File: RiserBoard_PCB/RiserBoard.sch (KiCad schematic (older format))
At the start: 11 parts, among them J1 BUS1, J2 Input, J3 BUS2

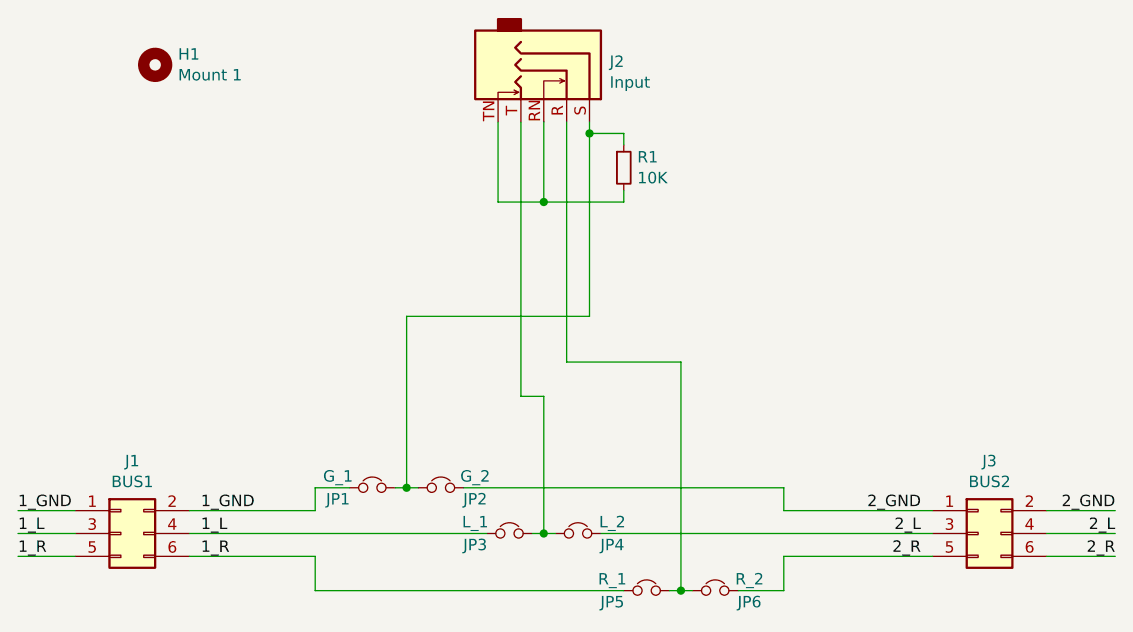
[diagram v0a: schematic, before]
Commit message: Updated Design to v0.1
Smaller PCB
Only 1 sided PCB
Different Jack Footprint
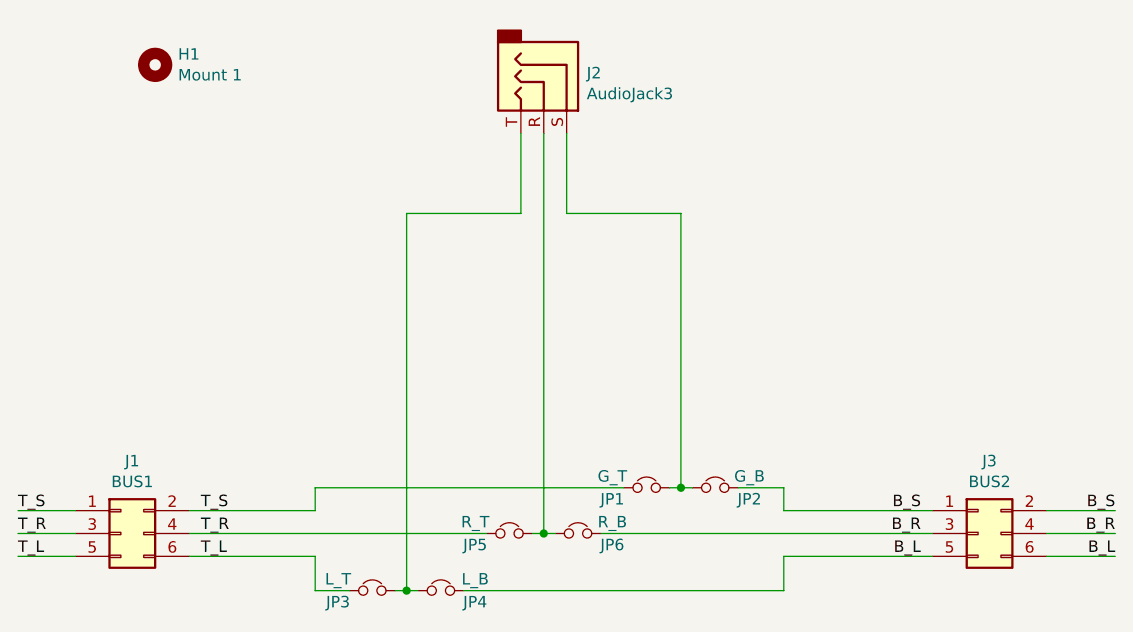
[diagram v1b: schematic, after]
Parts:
- removed J2: Input, Jack_3.5mm_Switchcraft_35RASMT4BHNTRX:Jack_3.5mm_Switchcraft_35RASMT4BHNTRX, symbol Connector:AudioJack3_SwitchTR
- removed R1: 10K, Resistor_SMD:R_0603_1608Metric, symbol Device:R_Small
- added J2: AudioJack3, Jack_3.5mm_PJ-313D-6A:PJ-313D-6A, symbol Connector:AudioJack3
- JP1: value G_1 -> G_T
- JP2: value G_2 -> G_B
- JP3: value L_1 -> L_T
- JP4: value L_2 -> L_B
- JP5: value R_1 -> R_T
- JP6: value R_2 -> R_B
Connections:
- net at JP1.2, JP2.1: now also J2.S
- net at JP3.2, JP4.1: now also J2.T
- net at JP5.2, JP6.1: now also J2.R
- net 1_GND renamed T_S
- net 1_L renamed T_R
- net T_R: now also JP5.1; no longer JP3.1
- net 1_R renamed T_L
- net T_L: now also JP3.1; no longer JP5.1
- net 2_GND renamed B_S
- net 2_L renamed B_R
- net B_R: now also JP6.2; no longer JP4.2
- net 2_R renamed B_L
- net B_L: now also JP4.2; no longer JP6.2
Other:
- moved on the sheet: JP1, JP2, JP3, JP4, JP5, JP6
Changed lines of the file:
@@
 	2950 4300 2700 4300
 Text Label 2700 4100 0    50   ~ 0
-1_GND
+T_S
 Text Label 2700 4200 0    50   ~ 0
-1_L
+T_R
 Text Label 2700 4300 0    50   ~ 0
-1_R
+T_L
 Text Label 3500 4100 0    50   ~ 0
-1_GND
+T_S
 Text Label 3500 4200 0    50   ~ 0
-1_L
+T_R
 Text Label 3500 4300 0    50   ~ 0
-1_R
+T_L
 Text Label 7500 4300 2    50   ~ 0
-2_R
-Text Label 7500 4200 2    50   ~ 0
-2_L
+B_L
 Text Label 7500 4100 2    50   ~ 0
-2_GND
+B_S
 Wire Wire Line
 	7200 4100 7500 4100
@@
 	7200 4300 7500 4300
 Text Label 6650 4300 2    50   ~ 0
-2_R
+B_L
 Text Label 6650 4200 2    50   ~ 0
-2_L
+B_R
 Text Label 6650 4100 2    50   ~ 0
-2_GND
-Wire Wire Line
-	4150 4000 4000 4000
+B_S
 Wire Wire Line
 	4000 4000 4000 4100
-Wire Wire Line
-	5350 4450 4000 4450
 Wire Wire Line
 	4000 4450 4000 4300
@@
 	6050 4000 6050 4100
 Wire Wire Line
-	6050 4450 6050 4300
-Wire Wire Line
 	3450 4100 4000 4100
-Wire Wire Line
-	3450 4200 4750 4200
 Wire Wire Line
 	3450 4300 4000 4300
@@
 L Device:Jumper_NC_Small JP1
 U 1 1 5E7C1BD8
-P 4250 4000
-F 0 "JP1" H 4100 3950 50  0000 C CNN
-F 1 "G_1" H 4100 4050 50  0000 C CNN
-F 2 "Resistor_SMD:R_0603_1608Metric" H 4250 4000 50  0001 C CNN
-F 3 "~" H 4250 4000 50  0001 C CNN
-	1    4250 4000
+P 5450 4000
+F 0 "JP1" H 5300 3950 50  0000 C CNN
+F 1 "G_T" H 5300 4050 50  0000 C CNN
+F 2 "Resistor_SMD:R_0603_1608Metric" H 5450 4000 50  0001 C CNN
+F 3 "~" H 5450 4000 50  0001 C CNN
+	1    5450 4000
 	1    0    0    -1
 $EndComp
@@
 L Device:Jumper_NC_Small JP2
 U 1 1 5E7C23FE
-P 4550 4000
-F 0 "JP2" H 4700 3950 50  0000 C CNN
-F 1 "G_2" H 4700 4050 50  0000 C CNN
-F 2 "Resistor_SMD:R_0603_1608Metric" H 4550 4000 50  0001 C CNN
-F 3 "~" H 4550 4000 50  0001 C CNN
-	1    4550 4000
+P 5750 4000
+F 0 "JP2" H 5900 3950 50  0000 C CNN
+F 1 "G_B" H 5900 4050 50  0000 C CNN
+F 2 "Resistor_SMD:R_0603_1608Metric" H 5750 4000 50  0001 C CNN
+F 3 "~" H 5750 4000 50  0001 C CNN
+	1    5750 4000
 	1    0    0    -1
 $EndComp
-Wire Wire Line
-	4350 4000 4400 4000
 $Comp
 L Device:Jumper_NC_Small JP3
 U 1 1 5E7C4C9C
+P 4250 4450
+F 0 "JP3" H 4100 4400 50  0000 C CNN
+F 1 "L_T" H 4100 4500 50  0000 C CNN
+F 2 "Resistor_SMD:R_0603_1608Metric" H 4250 4450 50  0001 C CNN
+F 3 "~" H 4250 4450 50  0001 C CNN
+	1    4250 4450
+	1    0    0    -1
+$EndComp
+$Comp
+L Device:Jumper_NC_Small JP4
+U 1 1 5E7C4CA2
+P 4550 4450
+F 0 "JP4" H 4700 4400 50  0000 C CNN
+F 1 "L_B" H 4700 4500 50  0000 C CNN
+F 2 "Resistor_SMD:R_0603_1608Metric" H 4550 4450 50  0001 C CNN
+F 3 "~" H 4550 4450 50  0001 C CNN
+	1    4550 4450
+	1    0    0    -1
+$EndComp
+$Comp
+L Device:Jumper_NC_Small JP5
+U 1 1 5E7C8F61
 P 4850 4200
-F 0 "JP3" H 4700 4150 50  0000 C CNN
-F 1 "L_1" H 4700 4250 50  0000 C CNN
+F 0 "JP5" H 4700 4150 50  0000 C CNN
+F 1 "R_T" H 4700 4250 50  0000 C CNN
 F 2 "Resistor_SMD:R_0603_1608Metric" H 4850 4200 50  0001 C CNN
 F 3 "~" H 4850 4200 50  0001 C CNN
@@
 $EndComp
 $Comp
-L Device:Jumper_NC_Small JP4
-U 1 1 5E7C4CA2
+L Device:Jumper_NC_Small JP6
+U 1 1 5E7C8F67
 P 5150 4200
-F 0 "JP4" H 5300 4150 50  0000 C CNN
-F 1 "L_2" H 5300 4250 50  0000 C CNN
+F 0 "JP6" H 5300 4150 50  0000 C CNN
+F 1 "R_B" H 5300 4250 50  0000 C CNN
 F 2 "Resistor_SMD:R_0603_1608Metric" H 5150 4200 50  0001 C CNN
 F 3 "~" H 5150 4200 50  0001 C CNN
@@
 	1    0    0    -1
 $EndComp
-$Comp
-L Device:Jumper_NC_Small JP5
-U 1 1 5E7C8F61
-P 5450 4450
-F 0 "JP5" H 5300 4400 50  0000 C CNN
-F 1 "R_1" H 5300 4500 50  0000 C CNN
-F 2 "Resistor_SMD:R_0603_1608Metric" H 5450 4450 50  0001 C CNN
-F 3 "~" H 5450 4450 50  0001 C CNN
-	1    5450 4450
-	1    0    0    -1
-$EndComp
-$Comp
-L Device:Jumper_NC_Small JP6
-U 1 1 5E7C8F67
-P 5750 4450
-F 0 "JP6" H 5900 4400 50  0000 C CNN
-F 1 "R_2" H 5900 4500 50  0000 C CNN
-F 2 "Resistor_SMD:R_0603_1608Metric" H 5750 4450 50  0001 C CNN
-F 3 "~" H 5750 4450 50  0001 C CNN
-	1    5750 4450
-	1    0    0    -1
-$EndComp
-Connection ~ 4400 4000
-Wire Wire Line
-	4400 4000 4450 4000
 $Comp
 L Connector_Generic:Conn_02x03_Odd_Even J1
@@
 	1    0    0    -1
 $EndComp
+$Comp
+L Connector:AudioJack3 J2
+U 1 1 5EC1880E
+P 5000 2250
+F 0 "J2" V 4936 2438 50  0000 L CNN
+F 1 "AudioJack3" V 5027 2438 50  0000 L CNN
+F 2 "Jack_3.5mm_PJ-313D-6A:PJ-313D-6A" H 5000 2250 50  0001 C CNN
+F 3 "~" H 5000 2250 50  0001 C CNN
+	1    5000 2250
+	0    1    1    0
+$EndComp
+Wire Wire Line
+	6050 4450 6050 4300
+Text Label 7500 4200 2    50   ~ 0
+B_R
+Wire Wire Line
+	5550 4000 5600 4000
+Wire Wire Line
+	4950 4200 5000 4200
+Wire Wire Line
+	4350 4450 4400 4450
+Wire Wire Line
+	4150 4450 4000 4450
+Wire Wire Line
+	3450 4200 4750 4200
+Wire Wire Line
+	4000 4000 5350 4000
 Wire Wire Line
 	5250 4200 6700 4200
 Wire Wire Line
-	6050 4000 4650 4000
+	6050 4000 5850 4000
 Wire Wire Line
-	6050 4450 5850 4450
-$Comp
-L Device:R_Small R1
-U 1 1 5E7E0BE6
-P 5350 2600
-F 0 "R1" H 5409 2646 50  0000 L CNN
-F 1 "10K" H 5409 2555 50  0000 L CNN
-F 2 "Resistor_SMD:R_0603_1608Metric" H 5350 2600 50  0001 C CNN
-F 3 "~" H 5350 2600 50  0001 C CNN
-	1    5350 2600
-	1    0    0    -1
-$EndComp
+	4650 4450 6050 4450
 Wire Wire Line
-	5200 2400 5200 2450
+	4400 4450 4400 2800
+Connection ~ 4400 4450
 Wire Wire Line
-	5350 2500 5350 2450
-Wire Wire Line
-	5350 2450 5200 2450
-Connection ~ 5200 2450
-Wire Wire Line
-	5350 2700 5350 2750
-Wire Wire Line
-	5350 2750 5000 2750
-Wire Wire Line
-	5000 2750 5000 2400
-Wire Wire Line
-	5000 2750 4800 2750
-Wire Wire Line
-	4800 2750 4800 2400
-Connection ~ 5000 2750
-$Comp
-L Connector:AudioJack3_SwitchTR J2
-U 1 1 5E7E9474
-P 5100 2200
-F 0 "J2" V 5036 2388 50  0000 L CNN
-F 1 "Input" V 5127 2388 50  0000 L CNN
-F 2 "Jack_3.5mm_Switchcraft_35RASMT4BHNTRX:Jack_3.5mm_Switchcraft_35RASMT4BHNTRX" H 5100 2200 50  0001 C CNN
-F 3 "~" H 5100 2200 50  0001 C CNN
-	1    5100 2200
-	0    1    1    0
-$EndComp
-Wire Wire Line
-	5200 3250 4400 3250
-Wire Wire Line
-	4400 3250 4400 4000
-Wire Wire Line
-	5200 2450 5200 3250
-Wire Wire Line
-	4950 4200 5000 4200
-Wire Wire Line
-	5550 4450 5600 4450
-Wire Wire Line
-	5000 3600 5000 4200
-Wire Wire Line
-	4900 2400 4900 3600
+	4400 4450 4450 4450
 Connection ~ 5000 4200
 Wire Wire Line
 	5000 4200 5050 4200
 Wire Wire Line
-	5600 4450 5600 3450
+	5000 2450 5000 4200
 Wire Wire Line
-	5600 3450 5100 3450
+	4400 2800 4900 2800
 Wire Wire Line
-	5100 2400 5100 3450
-Connection ~ 5600 4450
+	4900 2800 4900 2450
 Wire Wire Line
-	5600 4450 5650 4450
+	5100 2450 5100 2800
 Wire Wire Line
-	4900 3600 5000 3600
+	5100 2800 5600 2800
+Wire Wire Line
+	5600 2800 5600 4000
+Connection ~ 5600 4000
+Wire Wire Line
+	5600 4000 5650 4000
 $EndSCHEMATC
